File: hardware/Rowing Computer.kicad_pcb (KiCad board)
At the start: 2 copper layers, 51 x 60 mm, 59 parts, among them J1 USB_B_Micro, J2 SWD, J3 Conn_01x02, J4 Micro_SD_Card, J5 Conn_01x31, U1 BQ25895RTW, U2 LP5907MFX-3.3, U3 STM32F042K6Tx, U4 MMA8451QR1, U5 LM2731XMF

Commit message: iteration 2 of board with correct footprint sizes and fixes where solder mask was not applied between pads
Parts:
- L2: footprint Inductor_SMD:L_0603_1608Metric -> Inductor_SMD:L_0805_2012Metric
- moved U5 0.56 mm to (63.7, 35.6)
- moved C17 0.37 mm to (62.1, 37.9)
- moved L2 0.36 mm to (66.6, 37.9)
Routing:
- net GND: track 29.7 -> 31.8 mm
- net +3V8: track 57.3 -> 56.7 mm
- net Net-(C18-Pad2): track 6.22 -> 6.78 mm
- net Net-(D5-Pad2): track 3.64 -> 4.21 mm

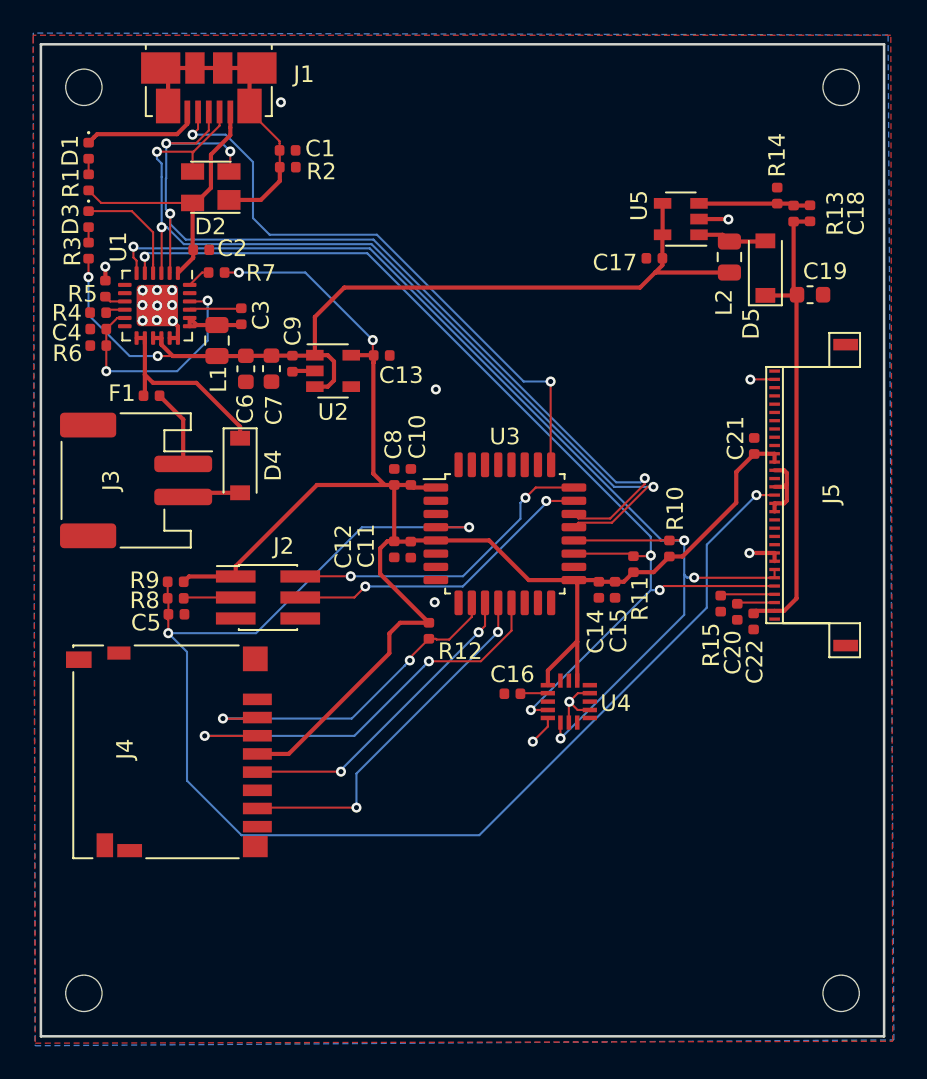
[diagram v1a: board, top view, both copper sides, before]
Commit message: Four layer design
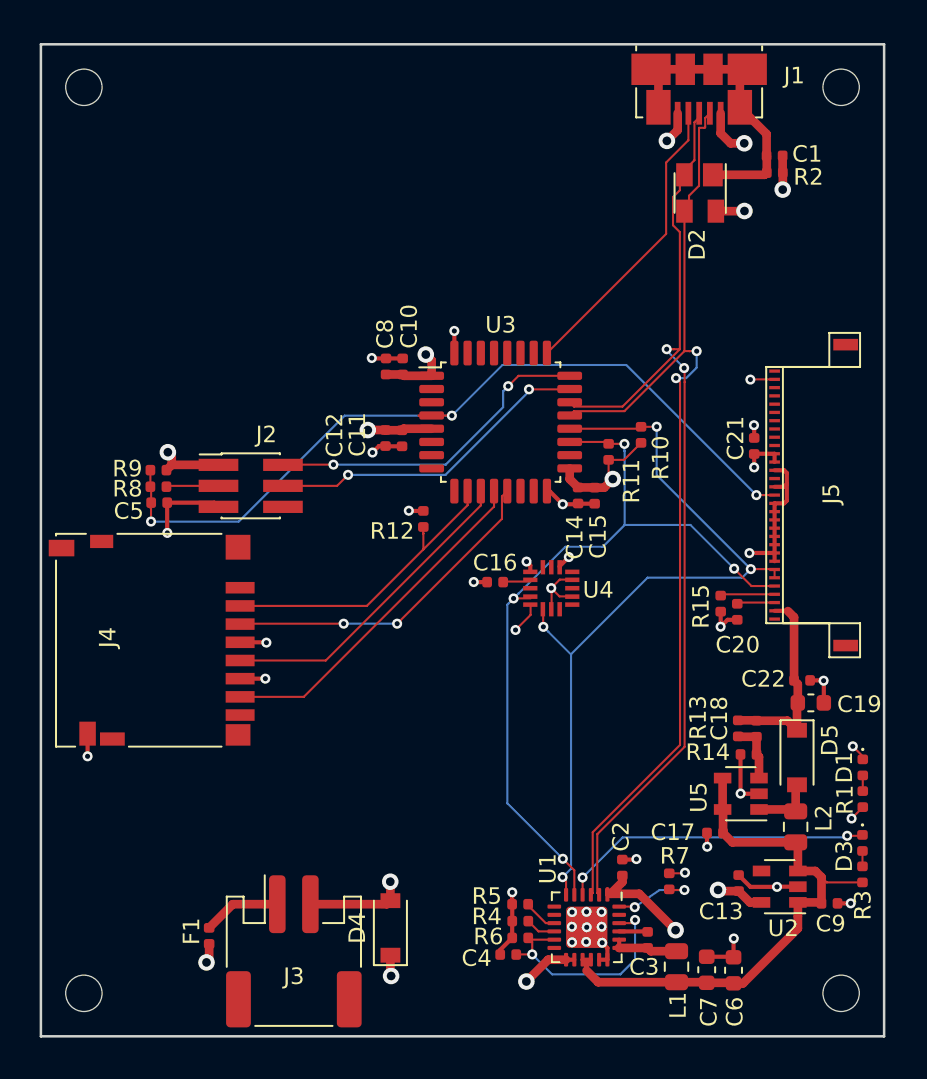
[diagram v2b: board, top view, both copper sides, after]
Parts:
- moved D3 60.1 mm to (74.7, 73.3)
- moved R3 60.1 mm to (74.7, 75.2)
- moved R1 59.9 mm to (74.7, 70.7)
- moved D1 59.9 mm to (74.7, 68.7)
- moved L1 47.0 mm to (63.4, 80.8)
- moved C6 46.8 mm to (66.9, 81.0), turned to 90 degrees
- moved C9 46.1 mm to (72.7, 77.0), turned to 0 degrees
- moved R7 45.9 mm to (63.0, 75.6), turned to 270 degrees
- moved U1 45.7 mm to (58.0, 78.4)
- moved C4 45.2 mm to (53.3, 80.1)
- moved C2 45.2 mm to (60.2, 74.8), turned to 90 degrees
- moved C3 45.0 mm to (61.7, 79.2)
- moved R5 44.9 mm to (54.0, 77.0), turned to 180 degrees
- moved C7 44.9 mm to (65.3, 81.0), turned to 90 degrees
- moved R4 44.8 mm to (54.0, 78.0)
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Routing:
- net +3V3: track 102.2 -> 30.4 mm, vias 2 -> 11
- net GND: track 31.8 -> 70.0 mm, vias 18 -> 35
- net /NRST: track 82.9 -> 49.9 mm
- net /SDA: track 71.1 -> 49.4 mm
- net +3V8: track 56.7 -> 35.1 mm, vias 2 -> 0
- net /OTG: track 36.4 -> 18.0 mm, vias 2 -> 0
- net /SCL: track 65.6 -> 48.2 mm
- net VCC: track 28.6 -> 12.1 mm
- net Net-(D3-Pad1): track 6.90 -> 19.0 mm, vias 0 -> 2
- net +BATT: track 11.8 -> 6.02 mm, vias 0 -> 3
- net /MOSI: track 26.1 -> 20.3 mm
- net +5V: track 17.8 -> 12.6 mm, vias 0 -> 4
- net /D-: track 56.6 -> 60.6 mm, vias 3 -> 2
- net /DSEL: track 1.45 -> 5.21 mm, vias 0 -> 2
- net Net-(C18-Pad2): track 6.78 -> 3.67 mm
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- added copper zone on InnnerBottom.Cu, net +3V3
- added copper zone on InnnerBottom.Cu, net +5V
- added copper zone on InnnerBottom.Cu, net +BATT
- added copper zone on InnerTop.Cu, net GND
- removed copper zone on B.Cu, net GND
- removed copper zone on F.Cu, net GND
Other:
- copper layers 2 -> 4
- net class Current: trace_width 0.254 -> 0.525; via_dia 0.6096 -> 1; via_drill 0.3048 -> 0.525
